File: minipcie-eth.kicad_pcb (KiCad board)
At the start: 4 copper layers, 75 x 86 mm, 36 parts, among them J1 PoE connector MainBoard, J2 PMOD I2C 6pin, J3 PoE connector addon, J4 PMOD UART 6pin, J5 PMOD UART 6pin, U1 VoCore_v2, U2 si3404, U3 ap2112, U4 MPCIE-Socket, X1 SI-52003-F

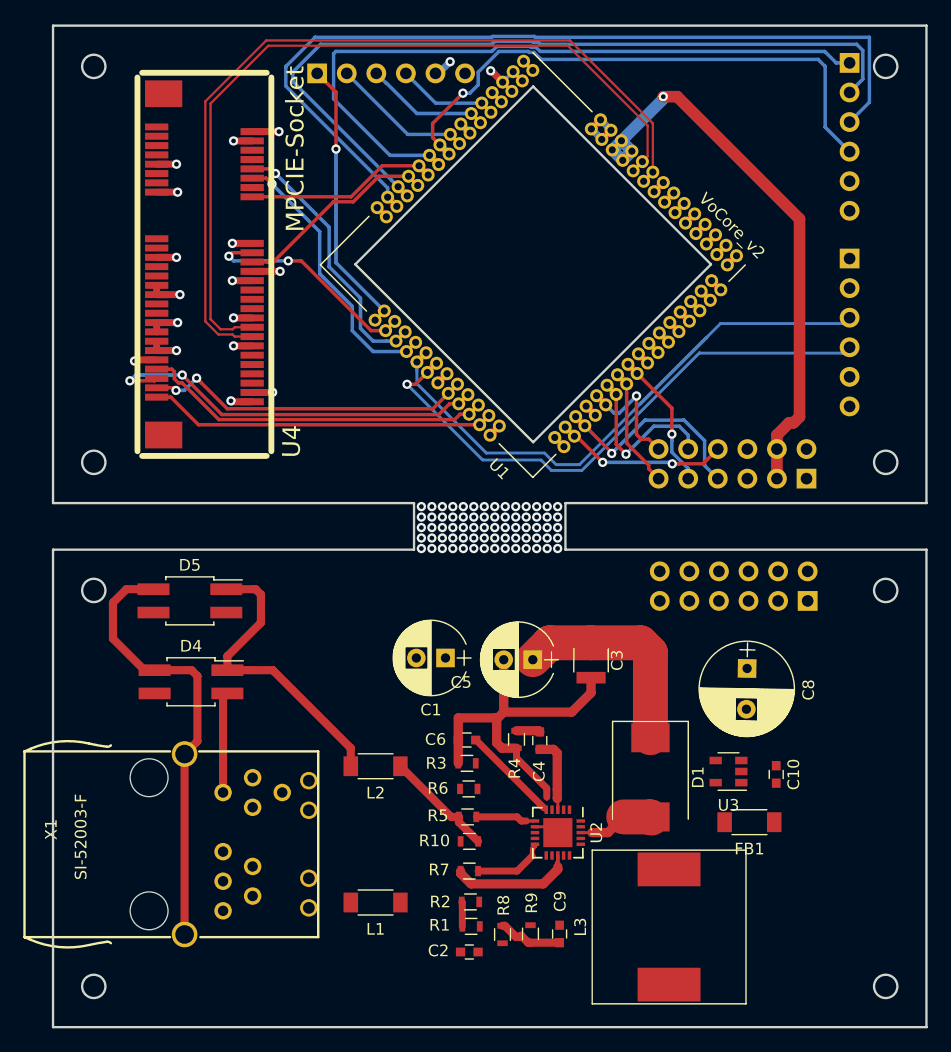
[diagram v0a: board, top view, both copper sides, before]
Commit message: No, go for si3404 first, the power budget is tight, but it can work and be significantly cheaper
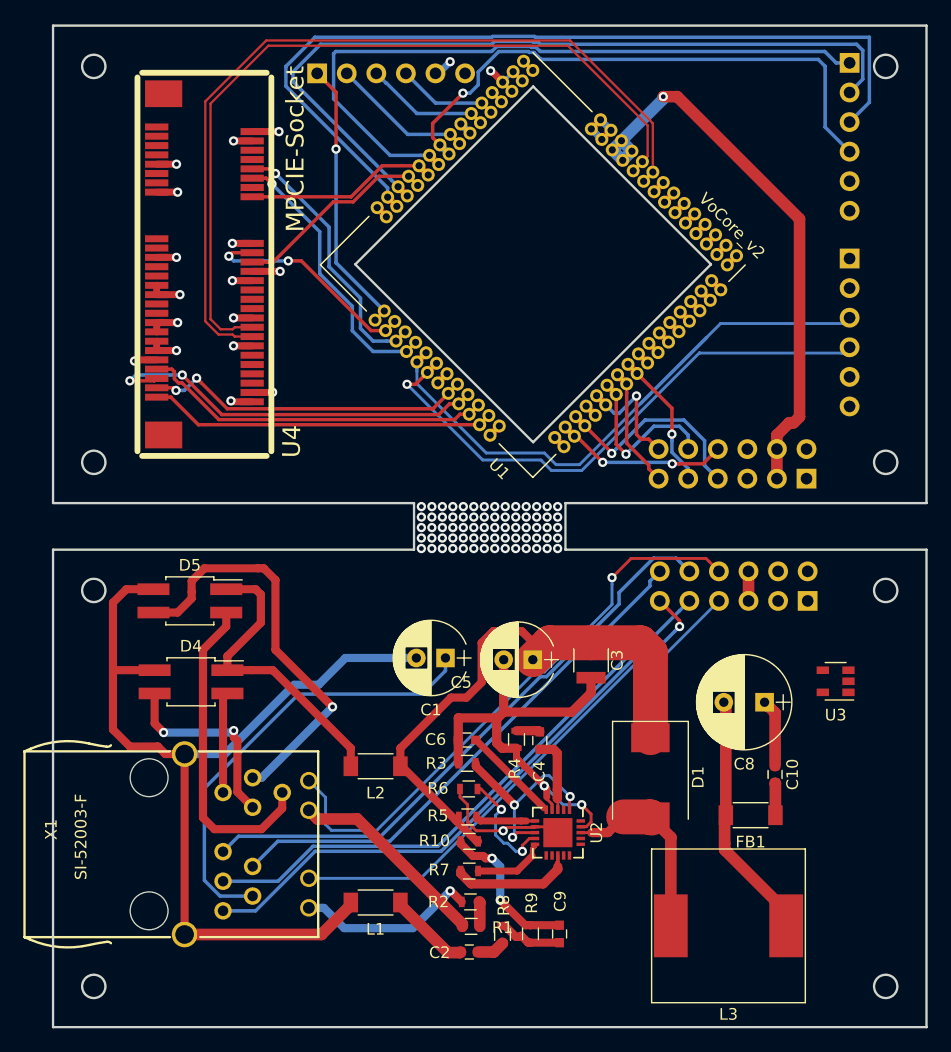
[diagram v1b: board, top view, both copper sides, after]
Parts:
- moved U3 12.0 mm to (178.1, 103.7)
- moved L3 5.10 mm to (168.9, 124.7), turned to 180 degrees
- moved C8 3.26 mm to (172.0, 105.5), turned to 180 degrees
- moved FB1 0.61 mm to (170.8, 115.2)
- moved C10 0.10 mm to (172.9, 111.7)
- turned R1 to 0 degrees
- turned R2 to 0 degrees
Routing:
- net /ethernet + POE/POTP: track 0.00 -> 52.2 mm, vias 0 -> 1
- net /ethernet + POE/PORN: track 0.00 -> 51.5 mm
- net /ethernet + POE/POTN: track 0.00 -> 50.0 mm
- net /ethernet + POE/LED2: track 0.00 -> 49.8 mm, vias 0 -> 1
- net /ethernet + POE/PORP: track 0.00 -> 45.7 mm
- net /ethernet + POE/LED1: track 0.00 -> 45.1 mm
- net Net-(C1-Pad2): track 40.4 -> 81.9 mm
- net Net-(C1-Pad1): track 0.00 -> 38.6 mm
- net Net-(D5-Pad4): track 0.00 -> 35.6 mm, vias 0 -> 1
- net /ethernet + POE/5V+_POE: track 30.1 -> 59.4 mm
- net Net-(D5-Pad3): track 0.00 -> 27.8 mm
- net Net-(C8-Pad2): track 0.00 -> 20.9 mm
- net Net-(R3-Pad2): track 0.00 -> 17.6 mm, vias 0 -> 3
- net Net-(R1-Pad1): track 0.00 -> 17.4 mm
- net Net-(D4-Pad4): track 0.00 -> 17.0 mm, vias 0 -> 2
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- added copper zone on In2.Cu, net /ethernet + POE/3V3-_POE
- added copper zone on In2.Cu, net /ethernet + POE/5V+_POE

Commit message: Switch to 90 degree orientation of the VoCore2. Separate 2.54mm pin headers into two 6-pin connectors, separating data and power, ready to re-route
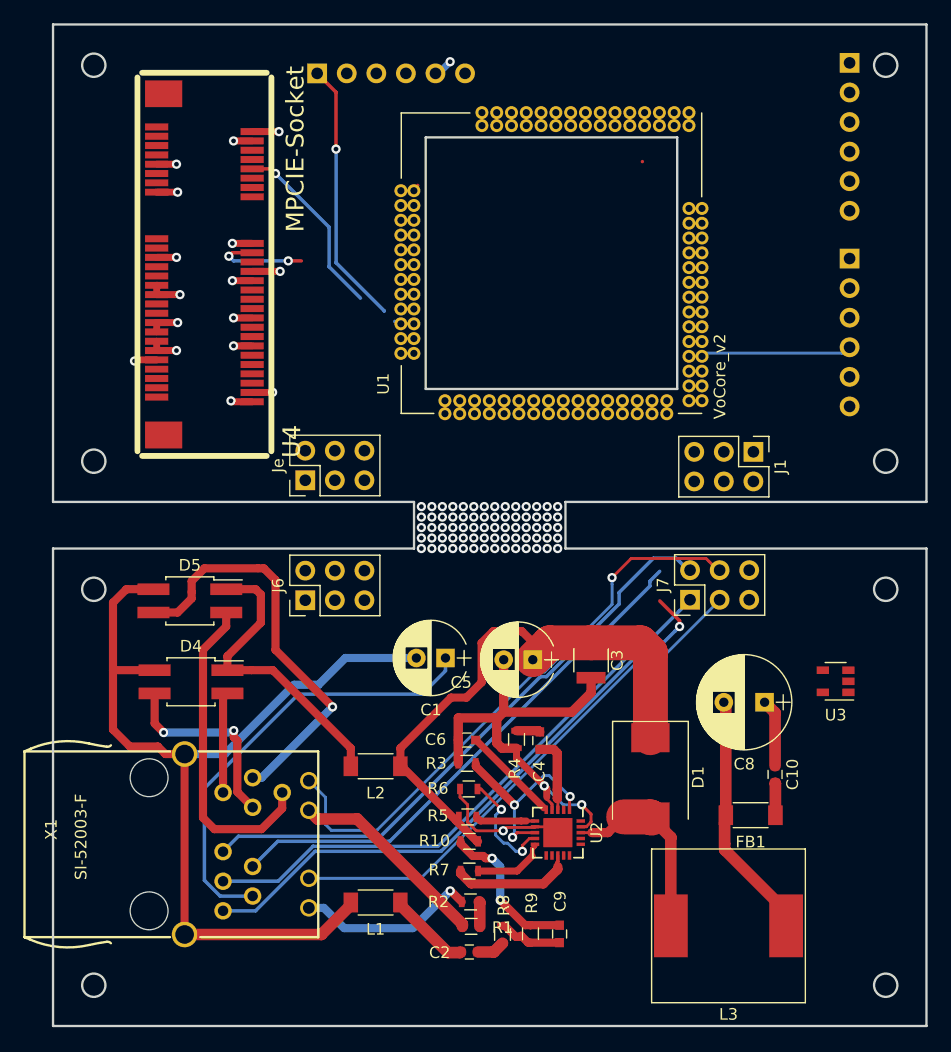
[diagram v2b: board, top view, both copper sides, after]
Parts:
- removed J3: PoE connector addon, Connector_PinHeader_2.54mm:PinHeader_2x06_P2.54mm_Vertical
- added J6: Conn_02x03_Odd_Even, Connector_PinHeader_2.54mm:PinHeader_2x03_P2.54mm_Vertical, F.Cu at (132.6, 96.7)
- added J7: Conn_02x03_Odd_Even, Connector_PinHeader_2.54mm:PinHeader_2x03_P2.54mm_Vertical, F.Cu at (165.6, 96.7)
- added Je: Conn_02x03_Odd_Even, Connector_PinHeader_2.54mm:PinHeader_2x03_P2.54mm_Vertical, F.Cu at (132.6, 86.4)
- J1: value PoE connector MainBoard -> Conn_02x03_Odd_Even; footprint Connector_PinHeader_2.54mm:PinHeader_2x06_P2.54mm_Vertical -> Connector_PinHeader_2.54mm:PinHeader_2x03_P2.54mm_Vertical; moved to F.Cu
- moved J1 5.11 mm to (171.0, 84.0), turned to 270 degrees
- moved U1 1.61 mm to (153.7, 67.8), turned to 90 degrees
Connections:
- J1 pad 1: GND -> +3V3
- J1 pad 2: GND -> +3V3
- J1 pad 5: +3V3 -> GND
- J1 pad 6: +3V3 -> GND
- U1 pad 2: Net-(J1-Pad8) -> Net-(J3-Pad5)
- U1 pad 3: Net-(J1-Pad7) -> Net-(J3-Pad6)
- U1 pad 5: Net-(J1-Pad12) -> Net-(J3-Pad1)
- U1 pad 6: Net-(J1-Pad10) -> Net-(J3-Pad3)
- U1 pad 7: Net-(J1-Pad11) -> Net-(J3-Pad2)
- U1 pad 8: Net-(J1-Pad9) -> Net-(J3-Pad4)
- U3 pad 5: /ethernet + POE/3V3+_POE -> (no net)
- X1 pad 1: /ethernet + POE/POTP -> (no net)
- X1 pad 3: /ethernet + POE/POTN -> (no net)
- X1 pad 4: /ethernet + POE/PORP -> (no net)
- X1 pad 5: /ethernet + POE/PORN -> (no net)
- X1 pad A1: /ethernet + POE/LED2 -> (no net)
- X1 pad A2: /ethernet + POE/LED1 -> (no net)
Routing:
- net (no net): track 0.00 -> 294.4 mm, vias 70 -> 68
- net Net-(J4-Pad3): track 75.1 -> 0.00 mm
- net /minipcie/USB_D+: track 72.3 -> 0.00 mm
- net /minipcie/USB_D-: track 69.4 -> 0.00 mm
- net Net-(J4-Pad2): track 69.1 -> 0.00 mm
- net Net-(J4-Pad1): track 60.4 -> 0.00 mm
- net /ethernet + POE/POTP: track 52.2 -> 0.00 mm, vias 1 -> 0
- net /ethernet + POE/PORN: track 51.5 -> 0.00 mm
- net /ethernet + POE/POTN: track 50.0 -> 0.00 mm
- net /ethernet + POE/LED2: track 49.8 -> 0.00 mm, vias 1 -> 0
- net +5V: track 49.4 -> 0.00 mm, vias 1 -> 0
- net Net-(J4-Pad4): track 48.8 -> 0.00 mm, vias 1 -> 0
- net Net-(J2-Pad3): track 48.0 -> 0.00 mm
- net /ethernet + POE/PORP: track 45.7 -> 0.00 mm
- net /ethernet + POE/LED1: track 45.1 -> 0.00 mm
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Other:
- outline, holes or cut-outs redrawn

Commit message: Rearrangement to 90 degrees for the VoCore and routing complete. Fighting last 5 DRC violations and then on to double-checking dimensions and clearances
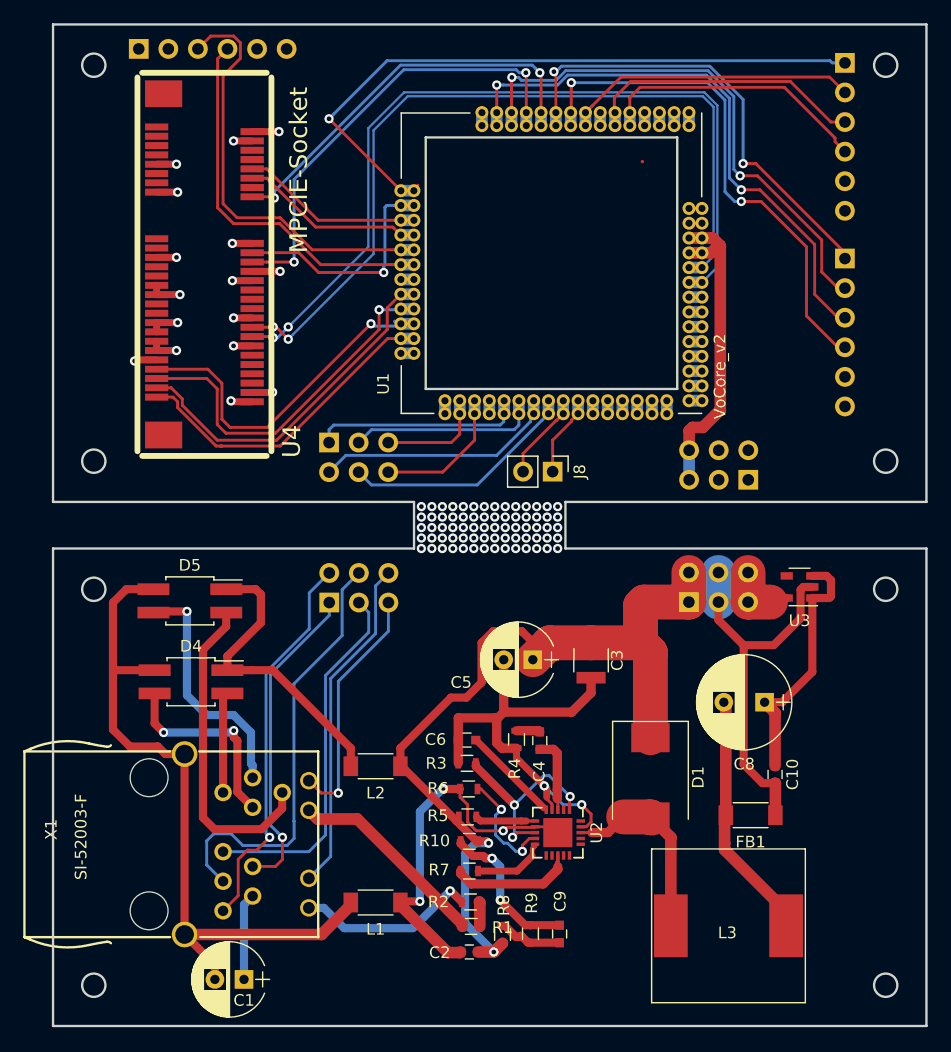
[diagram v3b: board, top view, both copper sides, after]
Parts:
- added J8: Conn_01x02, Connector_PinHeader_2.54mm:PinHeader_1x02_P2.54mm_Vertical, F.Cu at (153.8, 85.7)
- J1: moved to B.Cu
- J3: renamed from Je; moved to B.Cu
- J6, J7: footprint Connector_PinHeader_2.54mm:PinHeader_2x03_P2.54mm_Vertical -> Connector_PinSocket_2.54mm:PinSocket_2x03_P2.54mm_Vertical; moved to B.Cu
- moved J2 63.6 mm to (118.3, 49.4), turned to 270 degrees
- moved J5 45.3 mm to (178.9, 50.6), turned to 180 degrees
- moved C1 32.6 mm to (127.3, 129.3)
- moved J4 16.8 mm to (178.9, 67.4)
- moved U3 8.67 mm to (175.0, 95.6)
- moved J3 3.83 mm to (134.6, 83.2), turned to 270 degrees
- moved J1 2.44 mm to (170.6, 86.4), turned to 90 degrees
- moved J6 2.07 mm to (134.6, 96.9), turned to 270 degrees
- moved J7 0.22 mm to (165.5, 96.9), turned to 270 degrees
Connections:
- J1 pad 3: +5V -> GND
- J1 pad 4: +5V -> GND
- J1 pad 5: GND -> +5V
- J1 pad 6: GND -> +5V
- J7 pad 1: /ethernet + POE/3V3+_POE -> /ethernet + POE/5V+_POE
- J7 pad 2: /ethernet + POE/3V3+_POE -> /ethernet + POE/5V+_POE
- J7 pad 3: /ethernet + POE/5V+_POE -> /ethernet + POE/3V3-_POE
- J7 pad 4: /ethernet + POE/5V+_POE -> /ethernet + POE/3V3-_POE
- J7 pad 5: /ethernet + POE/3V3-_POE -> /ethernet + POE/3V3+_POE
- J7 pad 6: /ethernet + POE/3V3-_POE -> /ethernet + POE/3V3+_POE
- U3 pad 5: (no net) -> /ethernet + POE/3V3+_POE
- X1 pad 1: (no net) -> /ethernet + POE/POTP
- X1 pad 3: (no net) -> /ethernet + POE/POTN
- X1 pad 4: (no net) -> /ethernet + POE/PORP
- X1 pad 5: (no net) -> /ethernet + POE/PORN
- X1 pad A1: (no net) -> /ethernet + POE/LED2
- X1 pad A2: (no net) -> /ethernet + POE/LED1
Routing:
- net (no net): track 294.4 -> 0.00 mm, vias 68 -> 70
- net /minipcie/USB_D+: track 0.00 -> 72.0 mm, vias 0 -> 2
- net /minipcie/USB_D-: track 0.00 -> 70.6 mm, vias 0 -> 2
- net Net-(J4-Pad3): track 0.00 -> 49.1 mm, vias 0 -> 2
- net Net-(J4-Pad2): track 0.00 -> 46.5 mm, vias 0 -> 2
- net Net-(J4-Pad4): track 0.00 -> 45.8 mm, vias 0 -> 2
- net Net-(J4-Pad1): track 0.00 -> 40.9 mm, vias 0 -> 2
- net /minipcie/MCU_RESET: track 0.00 -> 39.2 mm, vias 0 -> 2
- net /ethernet + POE/5V+_POE: track 59.4 -> 98.6 mm, vias 0 -> 2
- net /ethernet + POE/POTN: track 0.00 -> 37.6 mm
- net Net-(J2-Pad3): track 0.00 -> 36.8 mm
- net /minipcie/MCU_PROG: track 0.00 -> 34.7 mm, vias 0 -> 2
- net /ethernet + POE/POTP: track 0.00 -> 33.5 mm, vias 0 -> 1
- net Net-(J5-Pad1): track 22.8 -> 56.3 mm
- net /ethernet + POE/PORN: track 0.00 -> 31.2 mm
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
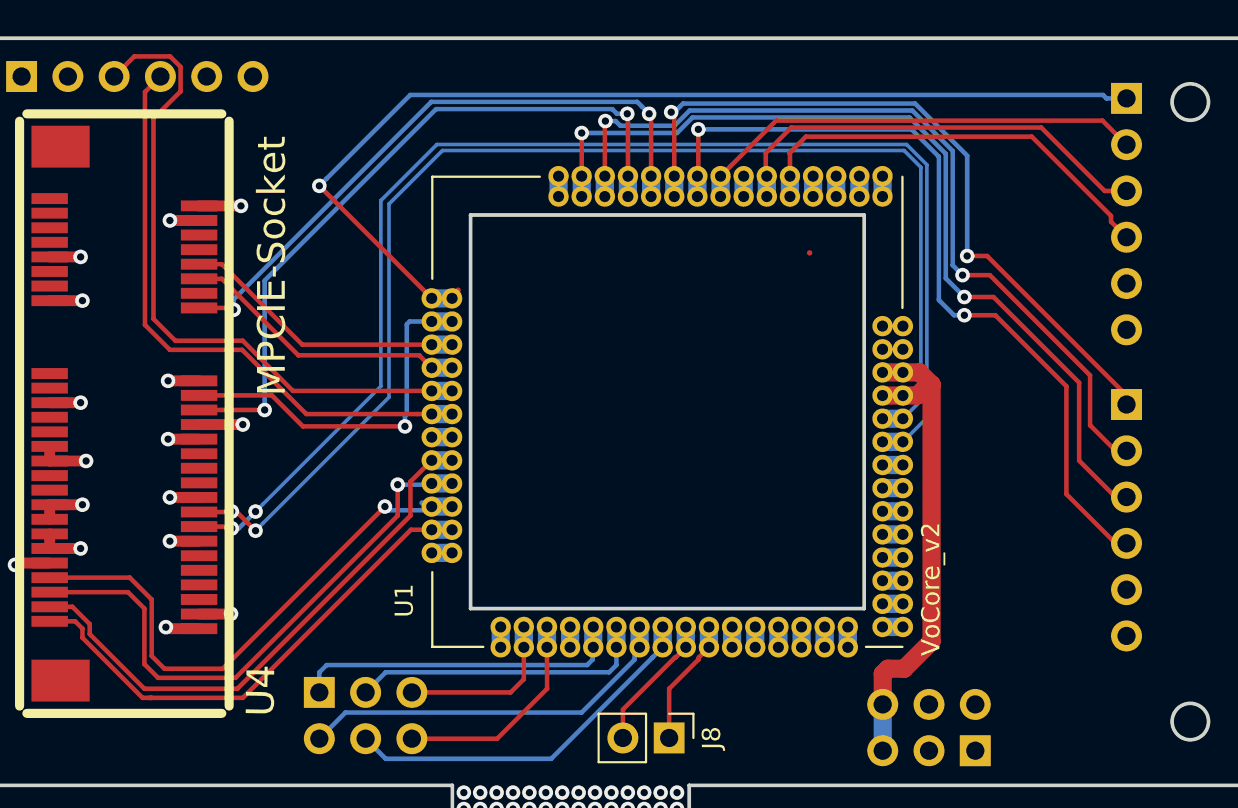
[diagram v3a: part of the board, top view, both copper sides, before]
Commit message: Re-routed USB_D- renaming pads so that the differential router did not get confused with multiple pads with the same name. Also removed ghost tracks for USB_D- and RF Kill
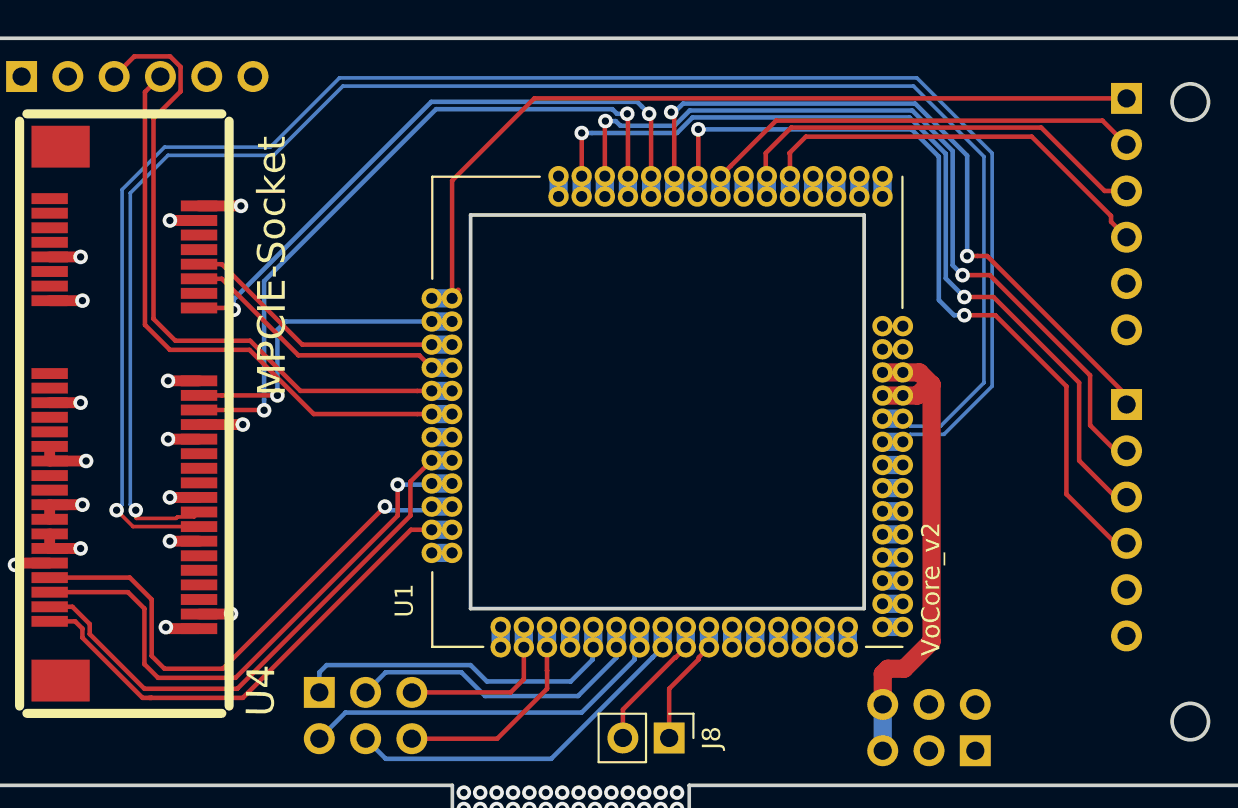
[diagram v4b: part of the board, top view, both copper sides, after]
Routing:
- net /minipcie/USB_D+: track 72.0 -> 94.7 mm, vias 2 -> 1
- net /minipcie/USB_D-: track 70.6 -> 91.6 mm, vias 2 -> 1
- net Net-(J5-Pad1): track 56.3 -> 46.5 mm, vias 1 -> 0
- net /minipcie/RF_KILL: track 20.2 -> 17.7 mm
- net Net-(J3-Pad3): track 16.5 -> 17.3 mm
- net Net-(J3-Pad1): track 18.2 -> 18.9 mm
- added copper zone on In1.Cu, net /ethernet + POE/3V3-_POE
- removed copper zone on In2.Cu, net /ethernet + POE/3V3-_POE
